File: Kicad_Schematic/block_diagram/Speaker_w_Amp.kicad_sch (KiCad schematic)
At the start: 2 parts

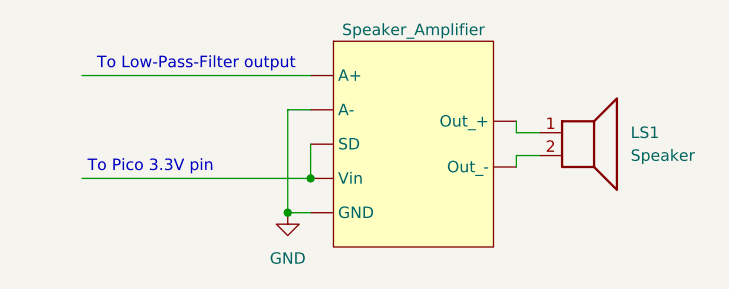
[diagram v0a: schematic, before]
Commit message: Updated mode select block for a 3rd button
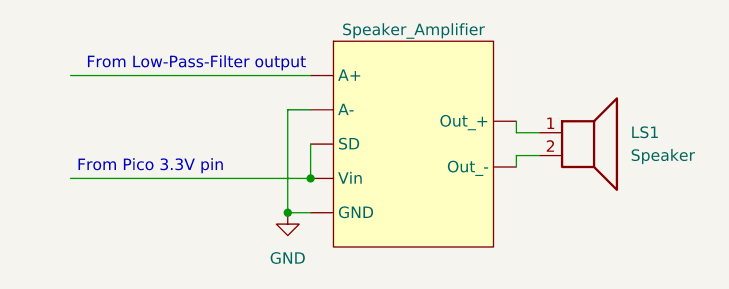
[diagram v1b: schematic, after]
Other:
- note added: "From Low-Pass-Filter output"
- note added: "From Pico 3.3V pin"
- note removed: "To Low-Pass-Filter output"
- note removed: "To Pico 3.3V pin"
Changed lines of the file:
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@@
 	(generator_version "9.0")
 	(paper "A4")
-	(text "To Pico 3.3V pin\n"
+	(text "From Pico 3.3V pin\n"
 		(exclude_from_sim no)
 		(at 101.6 99.06 0)
@@
 		)
 	)
-	(text "To Low-Pass-Filter output\n"
+	(text "From Low-Pass-Filter output\n"
 		(exclude_from_sim no)
 		(at 106.68 87.63 0)
@@
 	(wire
 		(pts
+			(xy 92.71 100.33) (xy 119.38 100.33)
+		)
+		(stroke
+			(width 0)
+			(type default)
+		)
+	)
+	(wire
+		(pts
 			(xy 119.38 96.52) (xy 119.38 100.33)
 		)
@@
 	(wire
 		(pts
-			(xy 93.98 100.33) (xy 119.38 100.33)
-		)
-		(stroke
-			(width 0)
-			(type default)
-		)
-	)
-	(wire
-		(pts
 			(xy 142.24 95.25) (xy 144.78 95.25)
 		)
@@
 	(wire
 		(pts
-			(xy 93.98 88.9) (xy 119.38 88.9)
+			(xy 92.71 88.9) (xy 119.38 88.9)
 		)
 		(stroke

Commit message: edited block diagrams from design rev 2
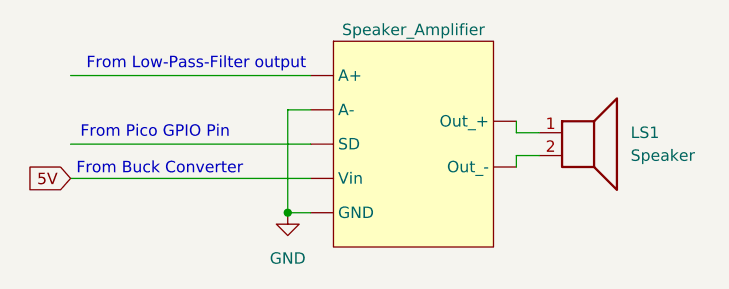
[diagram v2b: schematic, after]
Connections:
- new net 5V: Speaker_Amplifier. (Out_-)
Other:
- note added: "From Buck Converter"
- note added: "From Pico GPIO Pin"
- note removed: "From Pico 3.3V pin"
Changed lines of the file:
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@@
 	(generator_version "9.0")
 	(paper "A4")
-	(text "From Pico 3.3V pin\n"
+	(text "From Buck Converter\n\n"
 		(exclude_from_sim no)
-		(at 101.6 99.06 0)
+		(at 102.616 100.33 0)
+		(effects
+			(font
+				(size 1.27 1.27)
+			)
+		)
+	)
+	(text "From Pico GPIO Pin\n"
+		(exclude_from_sim no)
+		(at 102.108 95.25 0)
 		(effects
 			(font
@@
 		(color 0 0 0 0)
 	)
-	(junction
-		(at 119.38 100.33)
-		(diameter 0)
-		(color 0 0 0 0)
-	)
 	(wire
 		(pts
@@
 		(pts
 			(xy 116.84 92.71) (xy 116.84 104.14)
+		)
+		(stroke
+			(width 0)
+			(type default)
+		)
+	)
+	(wire
+		(pts
+			(xy 92.71 96.52) (xy 119.38 96.52)
 		)
 		(stroke
@@
 	(wire
 		(pts
-			(xy 119.38 96.52) (xy 119.38 100.33)
-		)
-		(stroke
-			(width 0)
-			(type default)
-		)
-	)
-	(wire
-		(pts
 			(xy 142.24 93.98) (xy 142.24 95.25)
 		)
@@
 		)
 	)
+	(global_label "5V"
+		(shape input)
+		(at 92.71 100.33 180)
+		(fields_autoplaced yes)
+		(effects
+			(font
+				(size 1.27 1.27)
+			)
+			(justify right)
+		)
+		(property "Intersheetrefs" "${INTERSHEET_REFS}"
+			(at 87.4267 100.33 0)
+			(effects
+				(font
+					(size 1.27 1.27)
+				)
+				(justify right)
+				(hide yes)
+			)
+		)
+	)
